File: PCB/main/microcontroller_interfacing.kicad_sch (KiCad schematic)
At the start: 12 parts, among them J6 USB_B_Micro, SW2 C13828, SW3 C13828

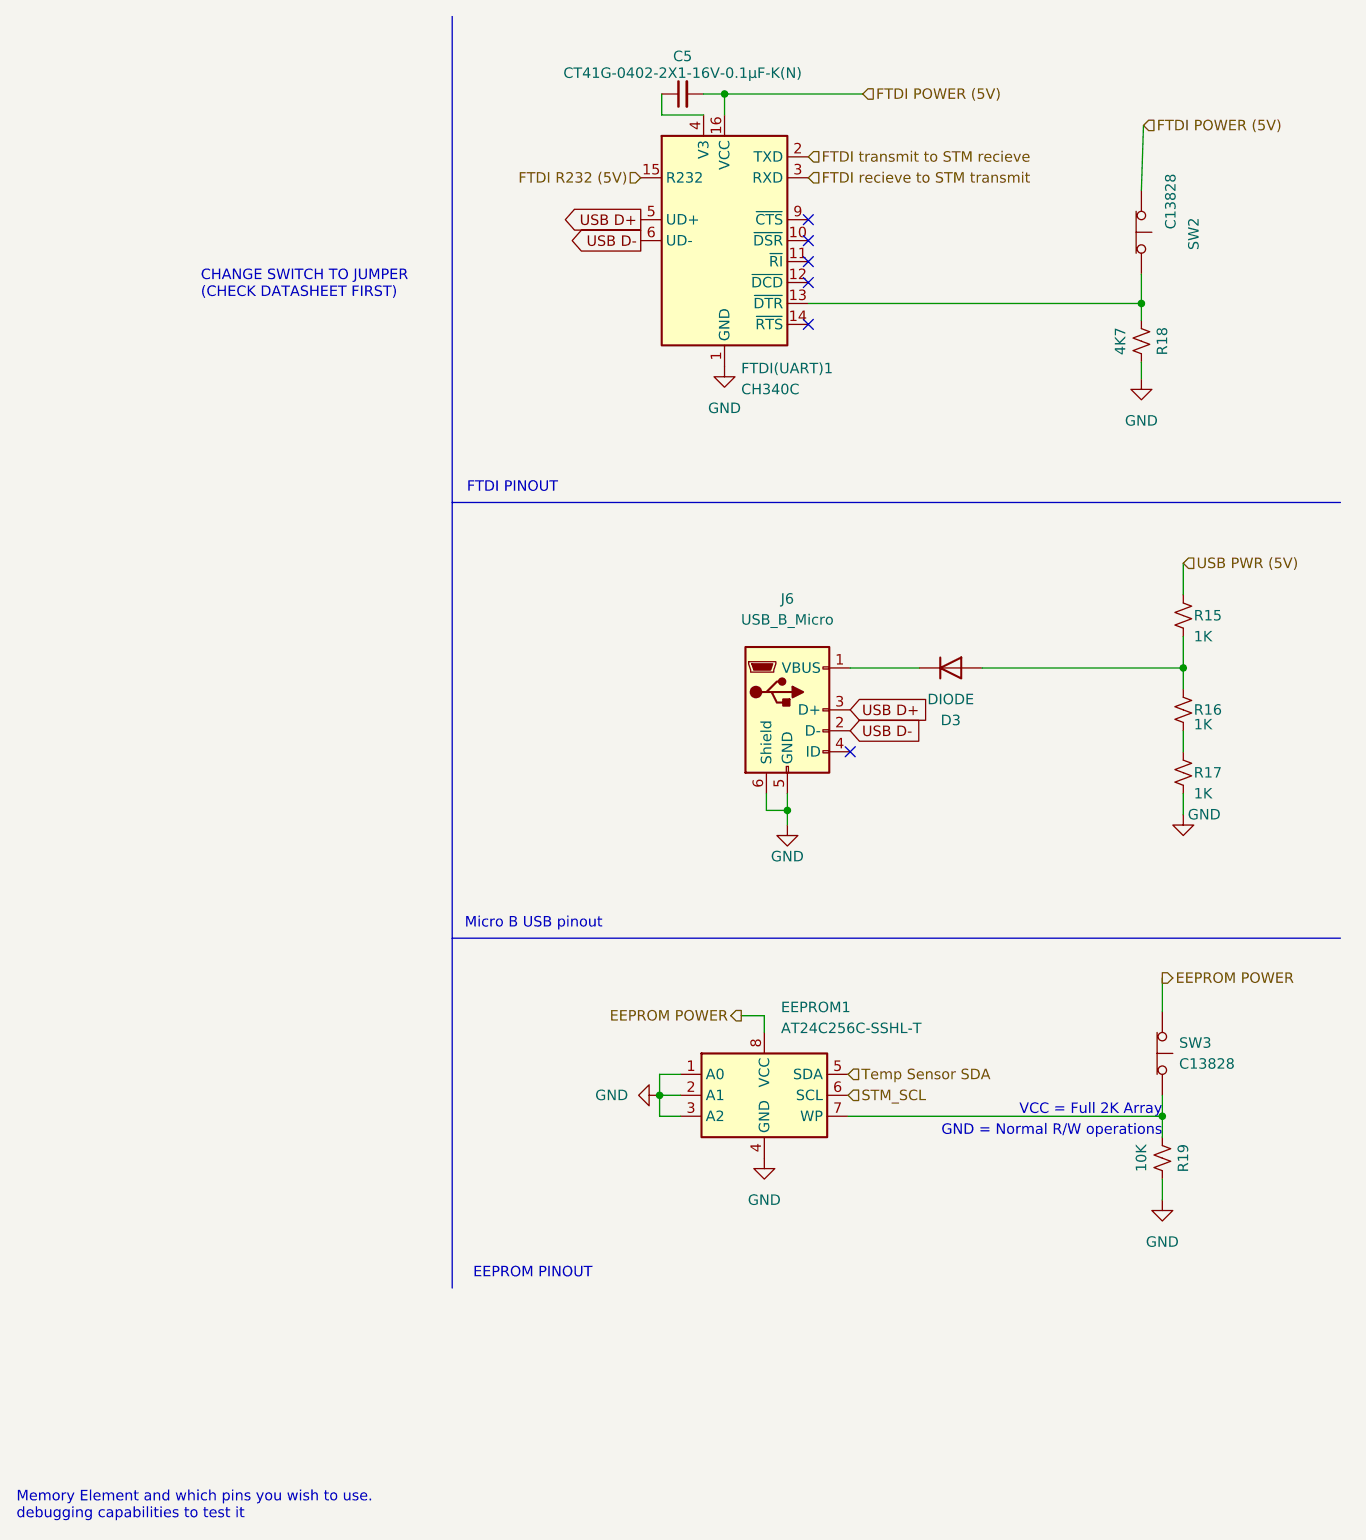
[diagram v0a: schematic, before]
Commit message: updated microcontroller schematic and added documentation
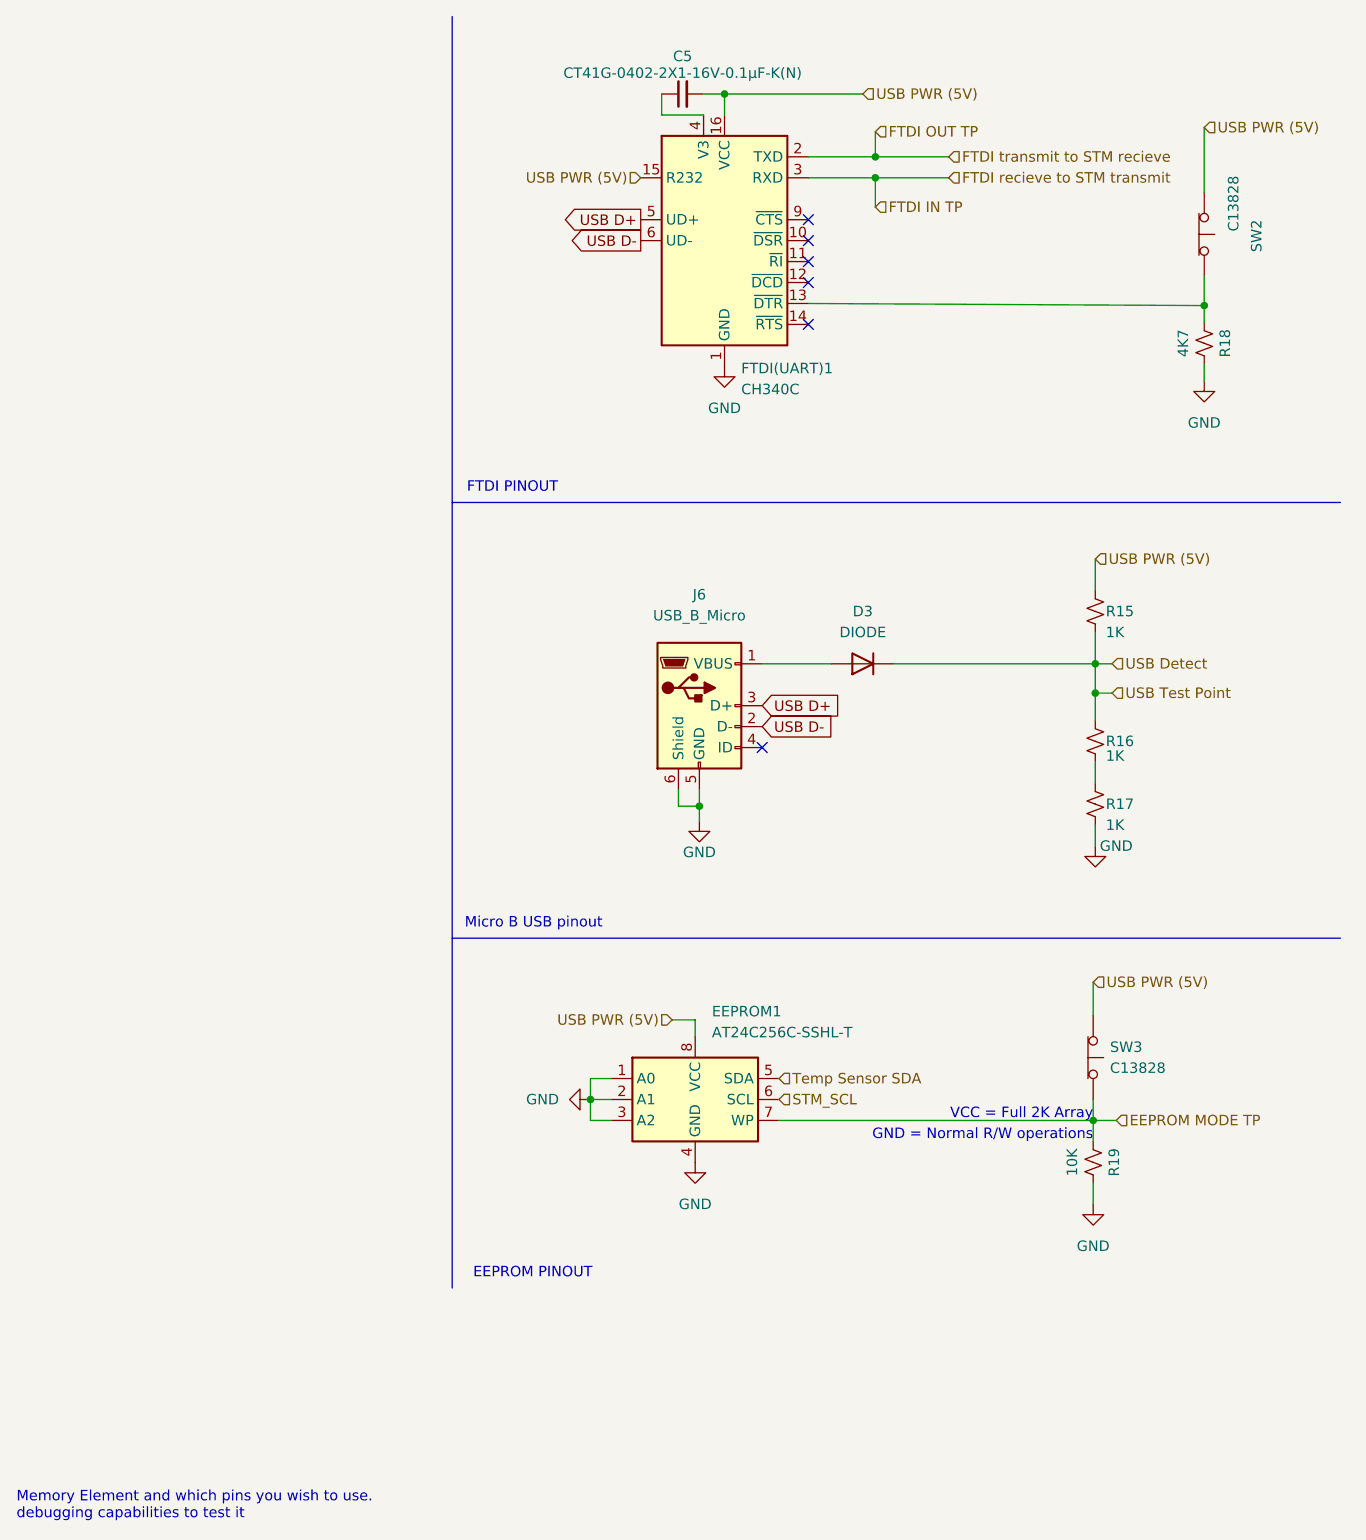
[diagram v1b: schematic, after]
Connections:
- net EEPROM POWER is gone; now on net USB PWR (5V): EEPROM1.8 (VCC), SW3.1 (A)
- net FTDI POWER (5V) is gone; now on net USB PWR (5V): C5.2, FTDI(UART)1.16 (VCC), SW2.1 (A)
- net FTDI R232 (5V) is gone; now on net USB PWR (5V): FTDI(UART)1.15 (R232)
- net USB Detect: now reaches R15.2, R16.1
- net USB Detect: now also D3.2 (K); no longer D3.1 (A)
- net EEPROM MODE TP: now reaches EEPROM1.7 (WP), R19.1, SW3.2 (B)
- net at J6.1 (VBUS): now also D3.1 (A); no longer D3.2 (K)
- net FTDI recieve to STM transmit renamed FTDI IN TP
- net FTDI transmit to STM recieve renamed FTDI OUT TP
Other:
- note removed: "CHANGE SWITCH TO JUMPER (CHECK DATASHEET FIRST)"
- moved on the sheet: D3, EEPROM1, J6, R15, R16, R17, R18, R19, SW2, SW3

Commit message: Replace microcontroller_interfacing.kicad_sch
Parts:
- renumbered C5 to C4, D3 to D4, J6 to J5, R19 to R14, SW3 to SW1
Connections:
- net FTDI IN TP renamed FTDI recieve to STM transmit
- net FTDI OUT TP renamed FTDI transmit to STM recieve
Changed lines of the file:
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@@
+    (effects (font (size 1.27 1.27)) (justify left bottom))
+  )
+  (label "FTDI OUT TP" (at 228.6 25.908 0)
+    (effects (font (size 1.27 1.27)) (justify left bottom))
+  )
+  (label "EEPROM MODE TP" (at 257.81 145.796 0)
+    (effects (font (size 1.27 1.27)) (justify left bottom))
+  )
+  (label "USB Test Point" (at 257.302 93.98 0)
+    (effects (font (size 1.27 1.27)) (justify left bottom))
+  )
+  (label "FTDI IN TP" (at 228.6 35.052 0)
     (effects (font (size 1.27 1.27)) (justify left bottom))
   )
@@
     (effects (font (size 1.27 1.27)) (justify left))
   )
-  (hierarchical_label "USB PWR (5V)" (shape input) (at 227.076 21.336 0)
+  (hierarchical_label "USB PWR (5V)" (shape output) (at 227.076 21.336 0)
     (effects (font (size 1.27 1.27)) (justify left))
   )
@@
     (effects (font (size 1.27 1.27)) (justify left))
   )
-  (hierarchical_label "FTDI IN TP" (shape input) (at 228.6 35.052 0)
-    (effects (font (size 1.27 1.27)) (justify left))
-  )
   (hierarchical_label "USB PWR (5V)" (shape input) (at 255.016 129.032 0)
     (effects (font (size 1.27 1.27)) (justify left))
@@
     (effects (font (size 1.27 1.27)) (justify left))
   )
-  (hierarchical_label "FTDI OUT TP" (shape input) (at 228.6 25.908 0)
-    (effects (font (size 1.27 1.27)) (justify left))
-  )
   (hierarchical_label "USB PWR (5V)" (shape input) (at 268.478 25.4 0)
     (effects (font (size 1.27 1.27)) (justify left))
   )
-  (hierarchical_label "USB Test Point" (shape input) (at 257.302 93.98 0)
-    (effects (font (size 1.27 1.27)) (justify left))
-  )
-  (hierarchical_label "EEPROM MODE TP" (shape input) (at 257.81 145.796 0)
-    (effects (font (size 1.27 1.27)) (justify left))
-  )
   (symbol (lib_id "power:GND") (at 255.27 112.522 0) (unit 1)
     (in_bom yes) (on_board yes)
-    (property "Reference" "#PWR037" (id 0) (at 255.27 118.872 0)
+    (property "Reference" "#PWR034" (id 0) (at 255.27 118.872 0)
       (effects (font (size 1.27 1.27)) hide)
     )
@@
   (symbol (lib_id "power:GND") (at 194.056 143.256 270) (unit 1)
     (in_bom yes) (on_board yes) (fields_autoplaced)
-    (property "Reference" "#PWR033" (id 0) (at 187.706 143.256 0)
+    (property "Reference" "#PWR029" (id 0) (at 187.706 143.256 0)
       (effects (font (size 1.27 1.27)) hide)
     )
@@
   (symbol (lib_id "power:GND") (at 268.478 56.134 0) (unit 1)
     (in_bom yes) (on_board yes) (fields_autoplaced)
-    (property "Reference" "#PWR039" (id 0) (at 268.478 62.484 0)
+    (property "Reference" "#PWR035" (id 0) (at 268.478 62.484 0)
       (effects (font (size 1.27 1.27)) hide)
     )
@@
   (symbol (lib_id "power:GND") (at 210.312 54.356 0) (unit 1)
     (in_bom yes) (on_board yes) (fields_autoplaced)
-    (property "Reference" "#PWR034" (id 0) (at 210.312 60.706 0)
+    (property "Reference" "#PWR032" (id 0) (at 210.312 60.706 0)
       (effects (font (size 1.27 1.27)) hide)
     )
@@
   (symbol (lib_id "Device:R_Small_US") (at 255.016 150.876 0) (unit 1)
     (in_bom yes) (on_board yes)
-    (property "Reference" "R19" (id 0) (at 257.556 150.876 90))
+    (property "Reference" "R14" (id 0) (at 257.556 150.876 90))
     (property "Value" "10K" (id 1) (at 252.476 150.876 90))
     (property "Footprint" "Resistor_SMD:R_0201_0603Metric" (id 2) (at 255.016 150.876 0)
@@
   (symbol (lib_id "power:GND") (at 207.264 109.474 0) (unit 1)
     (in_bom yes) (on_board yes)
-    (property "Reference" "#PWR036" (id 0) (at 207.264 115.824 0)
+    (property "Reference" "#PWR031" (id 0) (at 207.264 115.824 0)
       (effects (font (size 1.27 1.27)) hide)
     )
@@
   (symbol (lib_id "power:GND") (at 206.756 150.876 0) (unit 1)
     (in_bom yes) (on_board yes) (fields_autoplaced)
-    (property "Reference" "#PWR035" (id 0) (at 206.756 157.226 0)
+    (property "Reference" "#PWR030" (id 0) (at 206.756 157.226 0)
       (effects (font (size 1.27 1.27)) hide)
     )
@@
   (symbol (lib_id "Simulation_SPICE:DIODE") (at 227.076 90.424 0) (unit 1)
     (in_bom yes) (on_board yes)
-    (property "Reference" "D3" (id 0) (at 227.076 84.074 0))
+    (property "Reference" "D4" (id 0) (at 227.076 84.074 0))
     (property "Value" "DIODE" (id 1) (at 227.076 86.614 0))
     (property "Footprint" "LED_SMD:LED_0805_2012Metric" (id 2) (at 227.076 90.424 0)
@@
   (symbol (lib_id "power:GND") (at 255.016 155.956 0) (unit 1)
     (in_bom yes) (on_board yes) (fields_autoplaced)
-    (property "Reference" "#PWR041" (id 0) (at 255.016 162.306 0)
+    (property "Reference" "#PWR033" (id 0) (at 255.016 162.306 0)
       (effects (font (size 1.27 1.27)) hide)
     )
@@
   (symbol (lib_id "Device:C_Small") (at 205.232 21.336 90) (unit 1)
     (in_bom yes) (on_board yes)
-    (property "Reference" "C5" (id 0) (at 205.232 16.764 90))
+    (property "Reference" "C4" (id 0) (at 205.232 16.764 90))
     (property "Value" "CT41G-0402-2X1-16V-0.1μF-K(N)" (id 1) (at 205.232 18.796 90))
     (property "Footprint" "Capacitor_SMD:C_0201_0603Metric" (id 2) (at 205.232 21.336 0)
@@
   (symbol (lib_id "Connector:USB_B_Micro") (at 207.264 95.504 0) (unit 1)
     (in_bom yes) (on_board yes) (fields_autoplaced)
-    (property "Reference" "J6" (id 0) (at 207.264 82.042 0))
+    (property "Reference" "J5" (id 0) (at 207.264 82.042 0))
     (property "Value" "USB_B_Micro" (id 1) (at 207.264 84.582 0))
     (property "Footprint" "Connector_USB:USB_Micro-B_Amphenol_10103594-0001LF_Horizontal" (id 2) (at 211.074 96.774 0)
@@
   (symbol (lib_id "Switch:SW_Push_Open") (at 255.016 138.176 270) (unit 1)
     (in_bom yes) (on_board yes) (fields_autoplaced)
-    (property "Reference" "SW3" (id 0) (at 257.048 136.9059 90)
-      (effects (font (size 1.27 1.27)) (justify left))
-    )
+    (property "Reference" "SW1" (id 0) (at 257.048 136.9059 90)
+      (effects (font (size 1.27 1.27)) (justify left))
+    )

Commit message: updated microcontroller submodule
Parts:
- added R19, R20: 0, Resistor_SMD:R_0201_0603Metric, symbol Device:R_Small_US
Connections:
- net FTDI recieve to STM transmit: now also R19.1
- net FTDI transmit to STM recieve: now also R20.1
- net USB PWR (5V): no longer FTDI(UART)1.15 (R232)
- net USB Test Point: now reaches D4.1 (A), J5.1 (VBUS)
- new net FTDI IN TP: R19.2
- new net FTDI OUT TP: R20.2
- no-connect marks 6 -> 7
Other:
- note added: "Normally open"
- moved on the sheet: C4, D4
